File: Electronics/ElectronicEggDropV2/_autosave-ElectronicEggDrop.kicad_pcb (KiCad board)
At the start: 2 copper layers, 52.9 x 74.6 mm, 21 parts

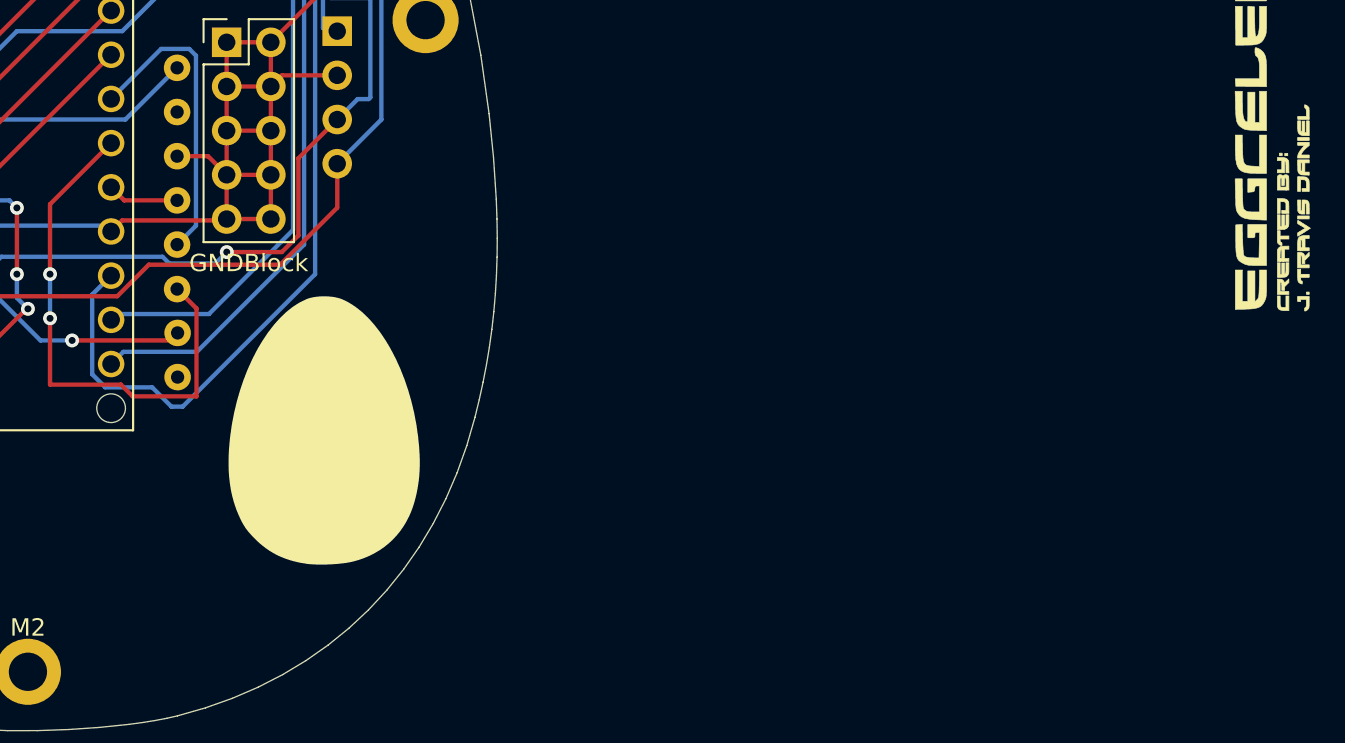
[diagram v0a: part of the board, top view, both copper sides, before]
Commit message: Updated v2, pretty much ready t order.  May experiment with reducing amountof spi wires used.
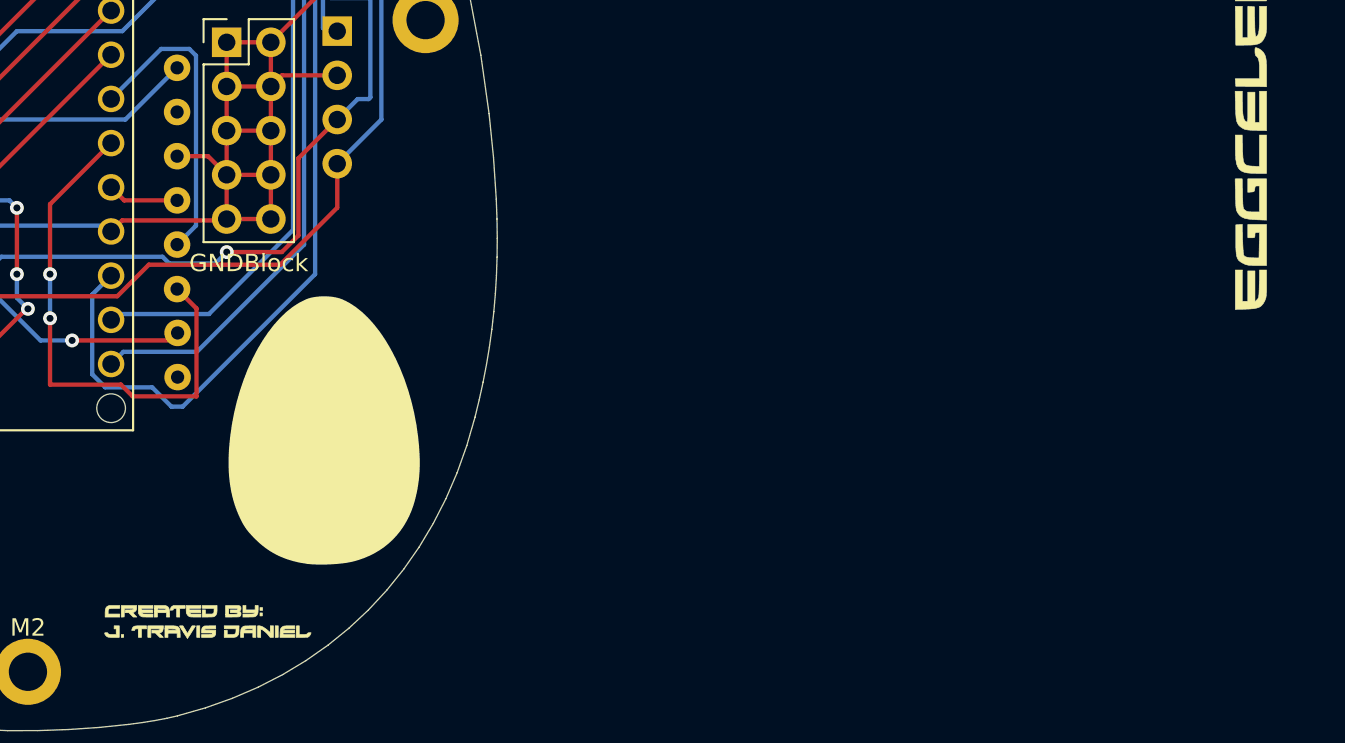
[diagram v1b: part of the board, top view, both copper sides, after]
